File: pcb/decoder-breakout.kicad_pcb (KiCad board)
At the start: 2 copper layers, 18 parts, among them J1 SM04B-SRSS-TB_LF__SN_, J2 SM04B-SRSS-TB_LF__SN_, J3 TBL009-254-08GY-2GY, Q1 BSS138, Q2 BSS138, U1 LS7866-S

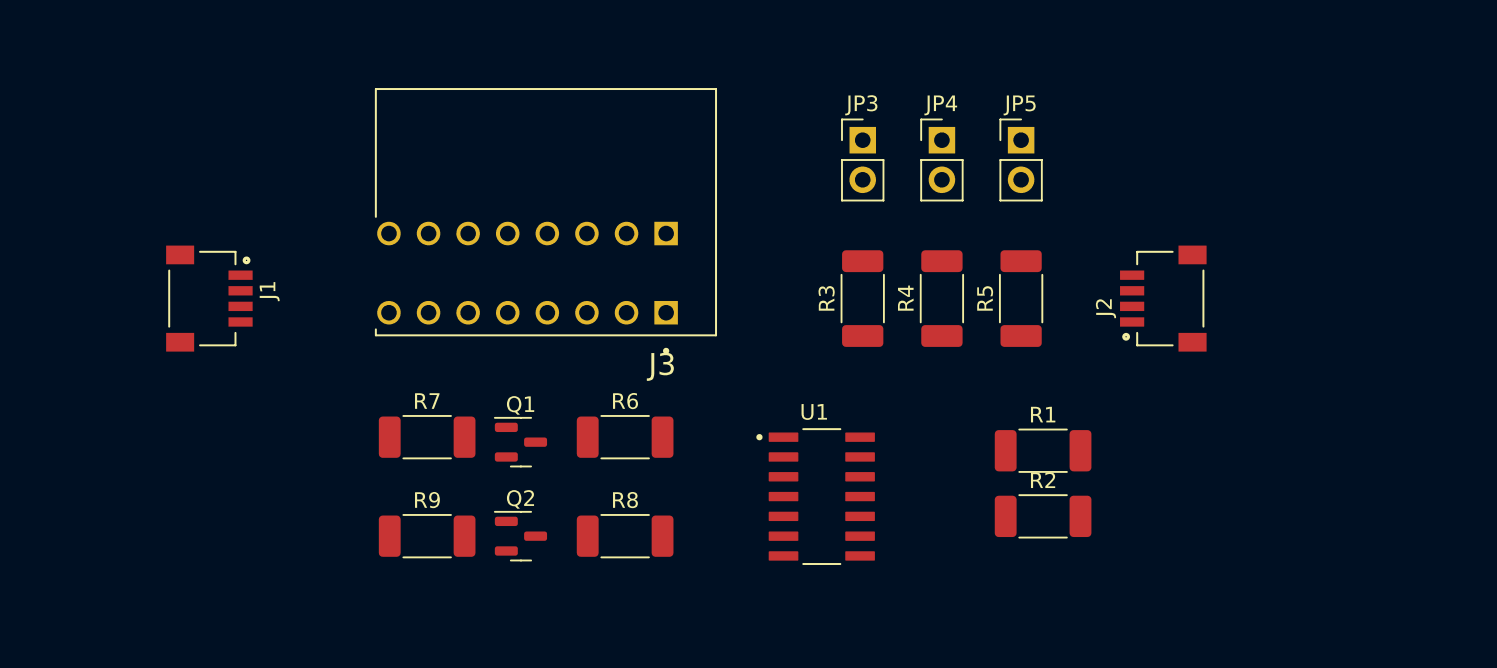
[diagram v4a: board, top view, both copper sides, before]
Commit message: pcb adding filled zones and starting connections
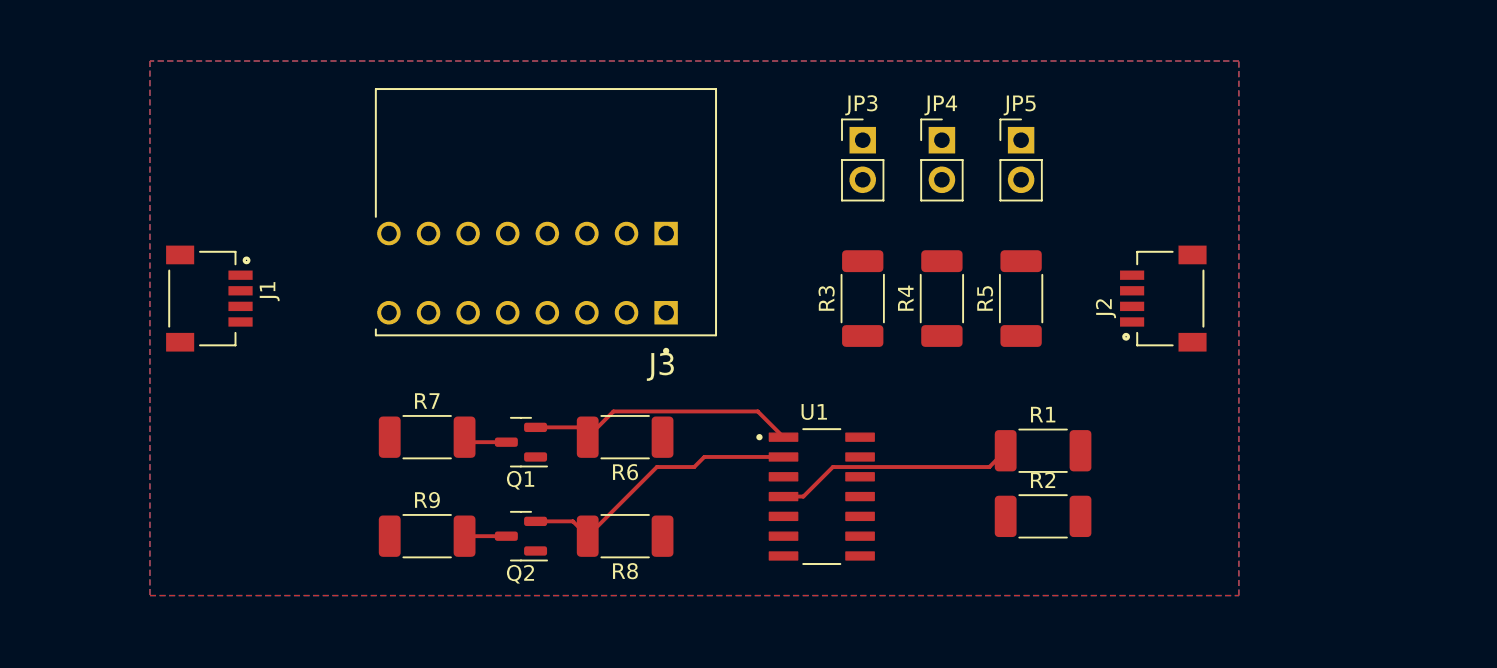
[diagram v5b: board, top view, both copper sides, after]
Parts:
- turned Q1 to 180 degrees
- turned Q2 to 180 degrees
- turned R6 to 180 degrees
- turned R8 to 180 degrees
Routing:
- net B: track 0.00 -> 18.4 mm
- net A: track 0.00 -> 17.5 mm
- net Net-(U1-CE): track 0.00 -> 15.5 mm
- net Encoder_A: track 0.00 -> 2.81 mm
- net Encoder_B: track 0.00 -> 2.68 mm
- added copper zone on B.Cu, net GND
- added copper zone on F.Cu, net VDD
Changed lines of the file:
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@@
   )
   (footprint "Package_TO_SOT_SMD:SOT-23" (layer "F.Cu")
-    (at 112.6975 106.68)
+    (at 112.6975 106.68 180)
     (descr "SOT, 3 Pin (https://www.jedec.org/system/files/docs/to-236h.pdf variant AB), generated with kicad-footprint-generator ipc_gullwing_generator.py")
     (tags "SOT TO_SOT_SMD")
@@
     (fp_line (start 0.65 1.45) (end -0.65 1.45)
       (stroke (width 0.1) (type solid)) (layer "F.Fab"))
-    (pad "1" smd roundrect (at -0.9375 -0.95) (size 1.475 0.6) (layers "F.Cu" "F.Paste" "F.Mask") (roundrect_rratio 0.25)
+    (pad "1" smd roundrect (at -0.9375 -0.95 180) (size 1.475 0.6) (layers "F.Cu" "F.Paste" "F.Mask") (roundrect_rratio 0.25)
       (net 2 "VDD") (pinfunction "G") (pintype "input"))
-    (pad "2" smd roundrect (at -0.9375 0.95) (size 1.475 0.6) (layers "F.Cu" "F.Paste" "F.Mask") (roundrect_rratio 0.25)
+    (pad "2" smd roundrect (at -0.9375 0.95 180) (size 1.475 0.6) (layers "F.Cu" "F.Paste" "F.Mask") (roundrect_rratio 0.25)
       (net 10 "B") (pinfunction "S") (pintype "passive"))
-    (pad "3" smd roundrect (at 0.9375 0) (size 1.475 0.6) (layers "F.Cu" "F.Paste" "F.Mask") (roundrect_rratio 0.25)
+    (pad "3" smd roundrect (at 0.9375 0 180) (size 1.475 0.6) (layers "F.Cu" "F.Paste" "F.Mask") (roundrect_rratio 0.25)
       (net 8 "Encoder_B") (pinfunction "D") (pintype "passive"))
     (model "${KICAD6_3DMODEL_DIR}/Package_TO_SOT_SMD.3dshapes/SOT-23.wrl"
@@
   )
   (footprint "Package_TO_SOT_SMD:SOT-23" (layer "F.Cu")
-    (at 112.6975 100.65)
+    (at 112.6975 100.65 180)
     (descr "SOT, 3 Pin (https://www.jedec.org/system/files/docs/to-236h.pdf variant AB), generated with kicad-footprint-generator ipc_gullwing_generator.py")
     (tags "SOT TO_SOT_SMD")
@@
     (fp_line (start 0.65 1.45) (end -0.65 1.45)
       (stroke (width 0.1) (type solid)) (layer "F.Fab"))
-    (pad "1" smd roundrect (at -0.9375 -0.95) (size 1.475 0.6) (layers "F.Cu" "F.Paste" "F.Mask") (roundrect_rratio 0.25)
+    (pad "1" smd roundrect (at -0.9375 -0.95 180) (size 1.475 0.6) (layers "F.Cu" "F.Paste" "F.Mask") (roundrect_rratio 0.25)
       (net 2 "VDD") (pinfunction "G") (pintype "input"))
-    (pad "2" smd roundrect (at -0.9375 0.95) (size 1.475 0.6) (layers "F.Cu" "F.Paste" "F.Mask") (roundrect_rratio 0.25)
+    (pad "2" smd roundrect (at -0.9375 0.95 180) (size 1.475 0.6) (layers "F.Cu" "F.Paste" "F.Mask") (roundrect_rratio 0.25)
       (net 9 "A") (pinfunction "S") (pintype "passive"))
-    (pad "3" smd roundrect (at 0.9375 0) (size 1.475 0.6) (layers "F.Cu" "F.Paste" "F.Mask") (roundrect_rratio 0.25)
+    (pad "3" smd roundrect (at 0.9375 0 180) (size 1.475 0.6) (layers "F.Cu" "F.Paste" "F.Mask") (roundrect_rratio 0.25)
       (net 7 "Encoder_A") (pinfunction "D") (pintype "passive"))
     (model "${KICAD6_3DMODEL_DIR}/Package_TO_SOT_SMD.3dshapes/SOT-23.wrl"
@@
   )
   (footprint "Resistor_SMD:R_2010_5025Metric_Pad1.40x2.65mm_HandSolder" (layer "F.Cu")
-    (at 119.38 106.68)
+    (at 119.38 106.68 180)
     (descr "Resistor SMD 2010 (5025 Metric), square (rectangular) end terminal, IPC_7351 nominal with elongated pad for handsoldering. (Body size source: IPC-SM-782 page 72, https://www.pcb-3d.com/wordpress/wp-content/uploads/ipc-sm-782a_amendment_1_and_2.pdf), generated with kicad-footprint-generator")
     (tags "resistor handsolder")
@@
     (fp_line (start 2.5 1.25) (end -2.5 1.25)
       (stroke (width 0.1) (type solid)) (layer "F.Fab"))
-    (pad "1" smd roundrect (at -2.4 0) (size 1.4 2.65) (layers "F.Cu" "F.Paste" "F.Mask") (roundrect_rratio 0.178571)
+    (pad "1" smd roundrect (at -2.4 0 180) (size 1.4 2.65) (layers "F.Cu" "F.Paste" "F.Mask") (roundrect_rratio 0.178571)
       (net 2 "VDD") (pintype "passive"))
-    (pad "2" smd roundrect (at 2.4 0) (size 1.4 2.65) (layers "F.Cu" "F.Paste" "F.Mask") (roundrect_rratio 0.178571)
+    (pad "2" smd roundrect (at 2.4 0 180) (size 1.4 2.65) (layers "F.Cu" "F.Paste" "F.Mask") (roundrect_rratio 0.178571)
       (net 10 "B") (pintype "passive"))
     (model "${KICAD6_3DMODEL_DIR}/Resistor_SMD.3dshapes/R_2010_5025Metric.wrl"
@@
   )
   (footprint "Resistor_SMD:R_2010_5025Metric_Pad1.40x2.65mm_HandSolder" (layer "F.Cu")
-    (at 119.38 100.33)
+    (at 119.38 100.33 180)
     (descr "Resistor SMD 2010 (5025 Metric), square (rectangular) end terminal, IPC_7351 nominal with elongated pad for handsoldering. (Body size source: IPC-SM-782 page 72, https://www.pcb-3d.com/wordpress/wp-content/uploads/ipc-sm-782a_amendment_1_and_2.pdf), generated with kicad-footprint-generator")
     (tags "resistor handsolder")
@@
     (fp_line (start 2.5 1.25) (end -2.5 1.25)
       (stroke (width 0.1) (type solid)) (layer "F.Fab"))
-    (pad "1" smd roundrect (at -2.4 0) (size 1.4 2.65) (layers "F.Cu" "F.Paste" "F.Mask") (roundrect_rratio 0.178571)
+    (pad "1" smd roundrect (at -2.4 0 180) (size 1.4 2.65) (layers "F.Cu" "F.Paste" "F.Mask") (roundrect_rratio 0.178571)
       (net 2 "VDD") (pintype "passive"))
-    (pad "2" smd roundrect (at 2.4 0) (size 1.4 2.65) (layers "F.Cu" "F.Paste" "F.Mask") (roundrect_rratio 0.178571)
+    (pad "2" smd roundrect (at 2.4 0 180) (size 1.4 2.65) (layers "F.Cu" "F.Paste" "F.Mask") (roundrect_rratio 0.178571)
       (net 9 "A") (pintype "passive"))
     (model "${KICAD6_3DMODEL_DIR}/Resistor_SMD.3dshapes/R_2010_5025Metric.wrl"
@@
     )
   )
+  (segment (start 111.76 100.65) (end 109.4 100.65) (width 0.25) (layer "F.Cu") (net 7))
+  (segment (start 109.4 100.65) (end 109.08 100.33) (width 0.25) (layer "F.Cu") (net 7))
+  (segment (start 111.76 106.68) (end 109.08 106.68) (width 0.25) (layer "F.Cu") (net 8))
+  (segment (start 127.89 98.68) (end 129.54 100.33) (width 0.25) (layer "F.Cu") (net 9))
+  (segment (start 113.635 99.7) (end 116.35 99.7) (width 0.25) (layer "F.Cu") (net 9))
+  (segment (start 116.35 99.7) (end 116.98 100.33) (width 0.25) (layer "F.Cu") (net 9))
+  (segment (start 116.98 100.33) (end 118.63 98.68) (width 0.25) (layer "F.Cu") (net 9))
+  (segment (start 118.63 98.68) (end 127.89 98.68) (width 0.25) (layer "F.Cu") (net 9))
+  (segment (start 121.415 102.245) (end 123.815 102.245) (width 0.25) (layer "F.Cu") (net 10))
+  (segment (start 113.635 105.73) (end 116.03 105.73) (width 0.25) (layer "F.Cu") (net 10))
+  (segment (start 124.46 101.6) (end 129.54 101.6) (width 0.25) (layer "F.Cu") (net 10))
+  (segment (start 123.815 102.245) (end 124.46 101.6) (width 0.25) (layer "F.Cu") (net 10))
+  (segment (start 116.03 105.73) (end 116.98 106.68) (width 0.25) (layer "F.Cu") (net 10))
+  (segment (start 116.98 106.68) (end 121.415 102.245) (width 0.25) (layer "F.Cu") (net 10))
+  (segment (start 132.705 102.245) (end 130.81 104.14) (width 0.25) (layer "F.Cu") (net 14))
+  (segment (start 142.745 102.245) (end 132.705 102.245) (width 0.25) (layer "F.Cu") (net 14))
+  (segment (start 130.81 104.14) (end 129.54 104.14) (width 0.25) (layer "F.Cu") (net 14))
+  (segment (start 143.79 101.2) (end 142.745 102.245) (width 0.25) (layer "F.Cu") (net 14))
+  (zone (net 2) (net_name "VDD") (layer "F.Cu") (hatch edge 0.5)
+    (priority 1)
+    (connect_pads (clearance 0.5))
+    (min_thickness 0.25) (filled_areas_thickness no)
+    (fill yes (thermal_gap 0.5) (thermal_bridge_width 0.5))
+    (polygon
+      (pts
+        (xy 88.9 76.2)
+        (xy 88.9 110.49)
+        (xy 158.75 110.49)
+        (xy 158.75 76.2)
+      )
+    )
+  )
+  (zone (net 1) (net_name "GND") (layer "B.Cu") (hatch edge 0.5)
+    (connect_pads (clearance 0.5))
+    (min_thickness 0.25) (filled_areas_thickness no)
+    (fill yes (thermal_gap 0.5) (thermal_bridge_width 0.5))
+    (polygon
+      (pts
+        (xy 88.9 76.2)
+        (xy 88.9 110.49)
+        (xy 158.75 110.49)
+        (xy 158.75 76.2)
+      )
+    )
+  )

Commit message: corrected jumper wiring
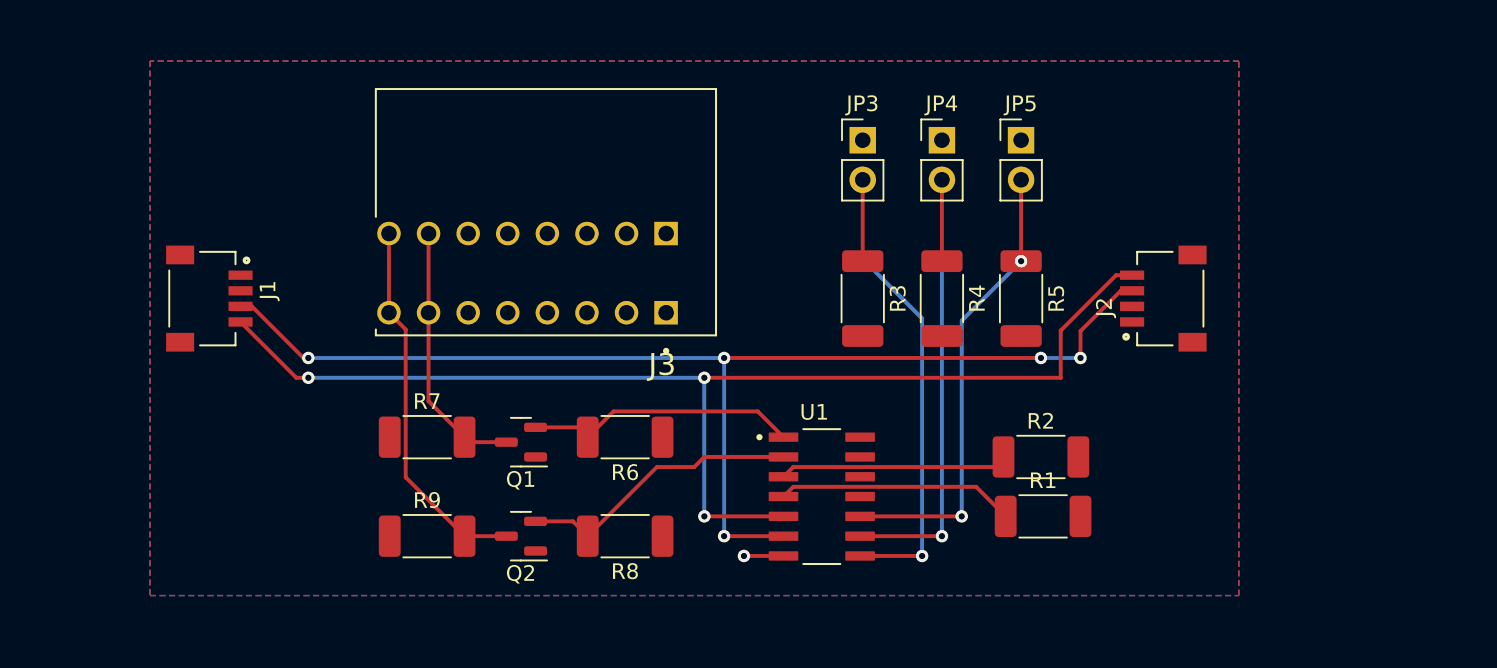
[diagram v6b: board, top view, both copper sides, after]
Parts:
- moved R1 4.21 mm to (146.2, 105.4)
- moved R2 3.81 mm to (146.1, 101.6)
- turned R3 to -90 degrees
- turned R4 to -90 degrees
- turned R5 to -90 degrees
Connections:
- JP3 pad 2: VDD -> Net-(JP3-B)
- JP4 pad 2: VDD -> Net-(JP4-B)
- JP5 pad 2: VDD -> Net-(JP5-B)
- R3 pad 1: Net-(U1-A0) -> Net-(JP3-B)
- R4 pad 1: Net-(U1-A1) -> Net-(JP4-B)
- R5 pad 1: Net-(U1-A2) -> Net-(JP5-B)
- U1 pad 10: Net-(U1-A2) -> Net-(JP5-B)
- U1 pad 8: Net-(U1-A0) -> Net-(JP3-B)
- U1 pad 9: Net-(U1-A1) -> Net-(JP4-B)
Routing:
- net Net-(U1-SCL): track 0.00 -> 77.1 mm, vias 0 -> 3
- net Net-(U1-SDA): track 0.00 -> 76.6 mm, vias 0 -> 5
- net Net-(JP3-B): track 0.00 -> 29.8 mm, vias 0 -> 1
- net Net-(JP5-B): track 0.00 -> 29.7 mm, vias 0 -> 2
- net Net-(JP4-B): track 0.00 -> 28.3 mm, vias 0 -> 1
- net Encoder_B: track 2.68 -> 24.1 mm
- net Net-(U1-Z): track 0.00 -> 14.6 mm
- net Encoder_A: track 2.81 -> 16.8 mm
- net GND: track 0.00 -> 2.54 mm, vias 0 -> 1

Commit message: clean up terminal block pins
- add 10 and 14 pin terminal blocks for possible use in the future
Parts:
- moved J1 8.11 mm to (86.6, 91.4)
- moved J3 7.61 mm to (114.4, 91.7)
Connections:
- J3 pad 4_A: Shield -> Encoder_A
- J3 pad 4_B: Shield -> Encoder_A
- J3 pad 5_A: GND -> Encoder_B
- J3 pad 5_B: GND -> Encoder_B
- J3 pad 7_A: Encoder_A -> GND
- J3 pad 7_B: Encoder_A -> GND
- J3 pad 8_A: Encoder_B -> Shield
- J3 pad 8_B: Encoder_B -> Shield
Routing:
- net Shield: track 0.00 -> 24.5 mm
- net Net-(U1-SDA): track 76.6 -> 84.7 mm
- net Net-(U1-SCL): track 77.1 -> 85.3 mm

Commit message: working on copper fill
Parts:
- JP3, JP4, JP5: value Jumper_2_Bridged -> (none)
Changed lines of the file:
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@@
         (effects (font (size 1 1) (thickness 0.15)))
     )
-    (fp_text value "Jumper_2_Bridged" (at 0 4.87) (layer "F.Fab")
+    (fp_text value " " (at 0 4.87) (layer "F.Fab")
         (effects (font (size 1 1) (thickness 0.15)))
     )
@@
         (effects (font (size 1 1) (thickness 0.15)))
     )
-    (fp_text value "Jumper_2_Bridged" (at 0 4.87) (layer "F.Fab")
+    (fp_text value " " (at 0 4.87) (layer "F.Fab")
         (effects (font (size 1 1) (thickness 0.15)))
     )
@@
         (effects (font (size 1 1) (thickness 0.15)))
     )
-    (fp_text value "Jumper_2_Bridged" (at 0 4.87) (layer "F.Fab")
+    (fp_text value " " (at 0 4.87) (layer "F.Fab")
         (effects (font (size 1 1) (thickness 0.15)))
     )
@@
   (segment (start 140.97 105.41) (end 140.97 92.85) (width 0.25) (layer "B.Cu") (net 18))
   (zone (net 2) (net_name "VDD") (layer "F.Cu") (hatch edge 0.5)
-    (priority 1)
     (connect_pads (clearance 0.5))
     (min_thickness 0.25) (filled_areas_thickness no)
@@
     (polygon
       (pts
-        (xy 81.4 76.35)
+        (xy 81.28 76.2)
         (xy 81.4 110.64)
         (xy 156.95 110.39)
@@
     (connect_pads (clearance 0.5))
     (min_thickness 0.25) (filled_areas_thickness no)
-    (fill (thermal_gap 0.5) (thermal_bridge_width 0.5))
+    (fill yes (thermal_gap 0.5) (thermal_bridge_width 0.5))
     (polygon
       (pts
